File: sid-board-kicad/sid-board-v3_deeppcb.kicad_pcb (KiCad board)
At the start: 2 copper layers, 50.8 x 50.8 mm, 49 parts, among them J1 SPI + UART, J2 USB_B_Micro, J3 UART, Q1 BSS138, Q2 BSS138, SW1 SW_EN, SW2 SW_FLASH, U1 SC16IS752IPW, U2 MCP1703A-3302_SOT223, U3 SN65HVD232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

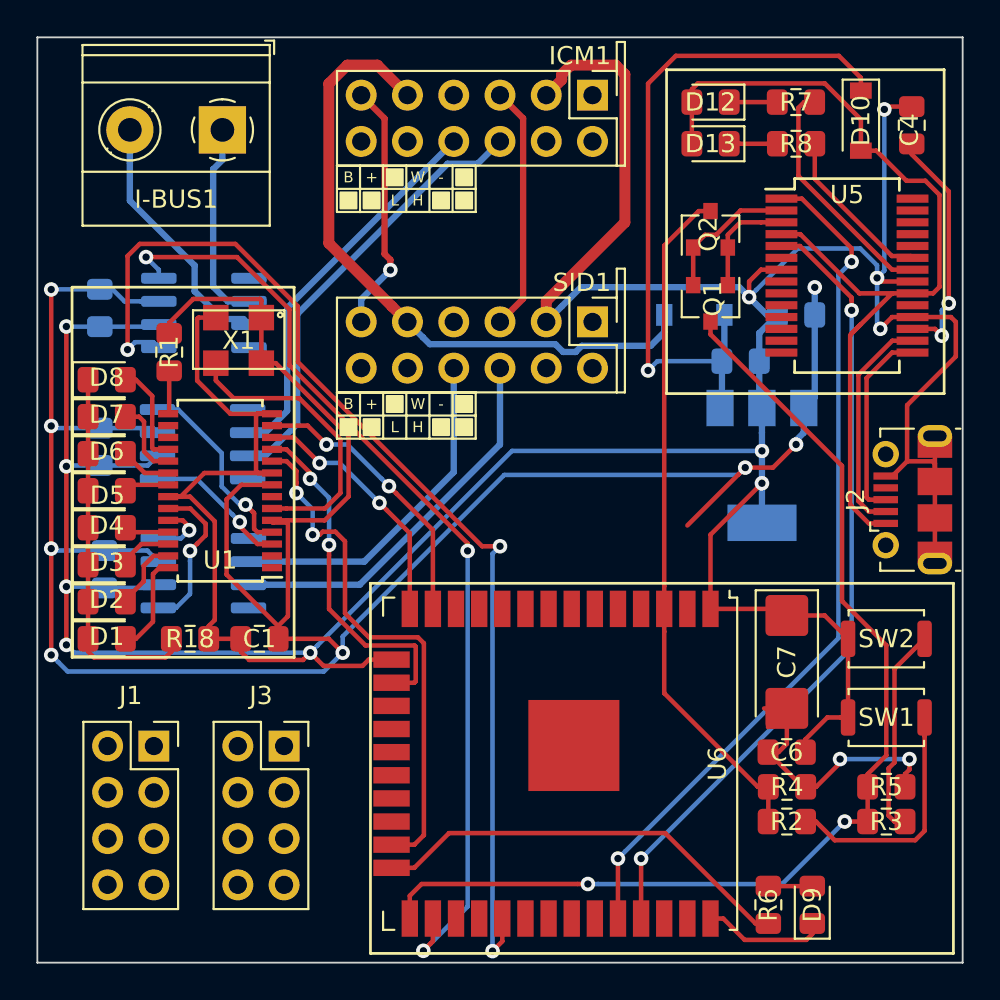
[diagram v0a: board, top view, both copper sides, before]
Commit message: Redid routing more logically
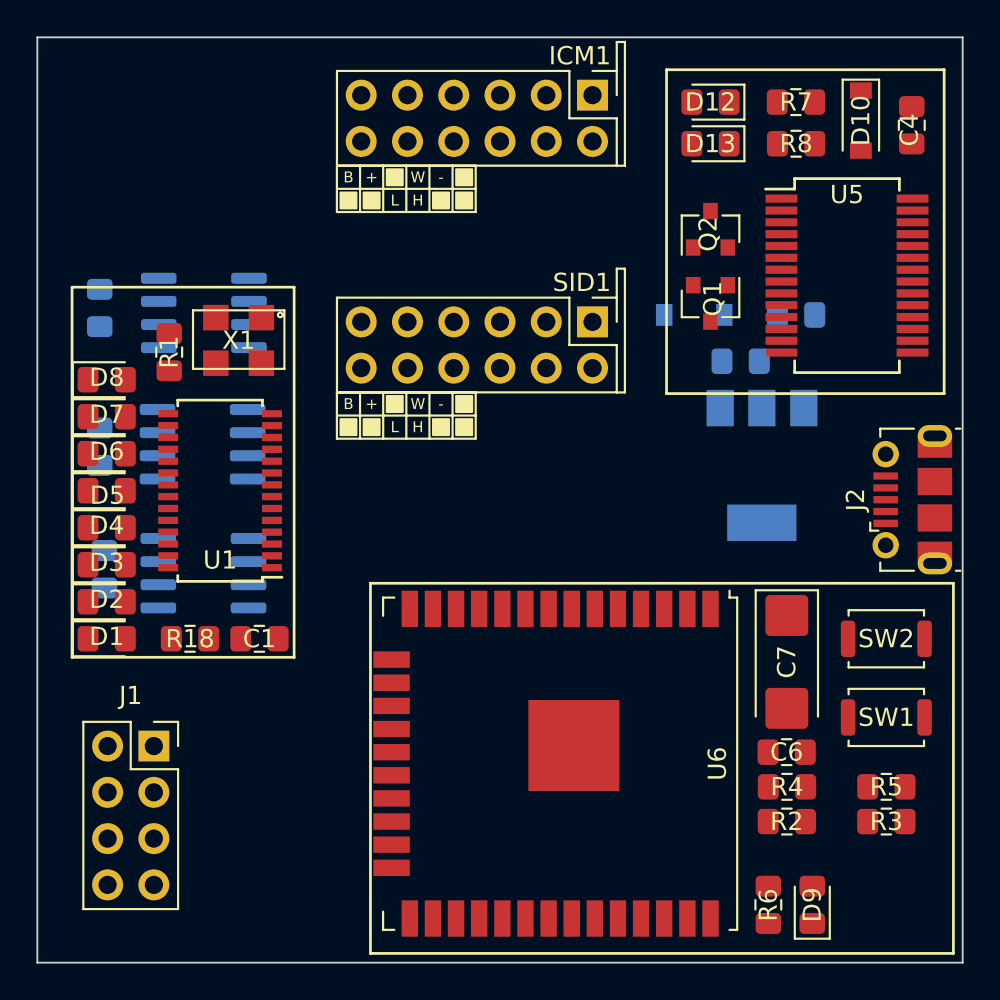
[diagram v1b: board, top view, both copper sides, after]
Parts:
- removed I-BUS1: Screw_Terminal_01x02, TerminalBlock_Phoenix:TerminalBlock_Phoenix_MKDS-1,5-2-5.08_1x02_P5.08mm_Horizontal
- removed J3: UART, Connector_PinSocket_2.54mm:PinSocket_2x04_P2.54mm_Vertical
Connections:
- U7 pad 6: CAN_L -> (no net)
- U7 pad 7: CAN_H -> (no net)
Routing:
- net GND: track 246.6 -> 0.00 mm, vias 11 -> 0
- net VDD_3.3V: track 162.4 -> 0.00 mm, vias 10 -> 0
- net TX_ESP32_CAN: track 60.9 -> 0.00 mm, vias 3 -> 0
- net IO0: track 59.9 -> 0.00 mm, vias 2 -> 0
- net RX_ESP32_CAN: track 52.8 -> 0.00 mm, vias 3 -> 0
- net VBUS: track 51.1 -> 0.00 mm
- net RX_ESP32: track 47.1 -> 0.00 mm, vias 2 -> 0
- net TX_ESP32: track 43.9 -> 0.00 mm, vias 2 -> 0
- net VIN: track 39.6 -> 0.00 mm, vias 1 -> 0
- net EN: track 37.7 -> 0.00 mm
- net Net-(D11-Pad2): track 36.5 -> 0.00 mm
- net CS: track 29.0 -> 0.00 mm, vias 2 -> 0
- net CAN_A_H: track 24.5 -> 0.00 mm
- net Net-(R6-Pad2): track 23.5 -> 0.00 mm
- net CAN_A_L: track 21.2 -> 0.00 mm
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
